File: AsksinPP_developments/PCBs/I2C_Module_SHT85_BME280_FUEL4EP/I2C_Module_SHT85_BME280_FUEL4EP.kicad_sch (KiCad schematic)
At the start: 14 parts, among them J1 Conn_01x04, J2 Conn_01x04, U1 BME280, U2 SHT85

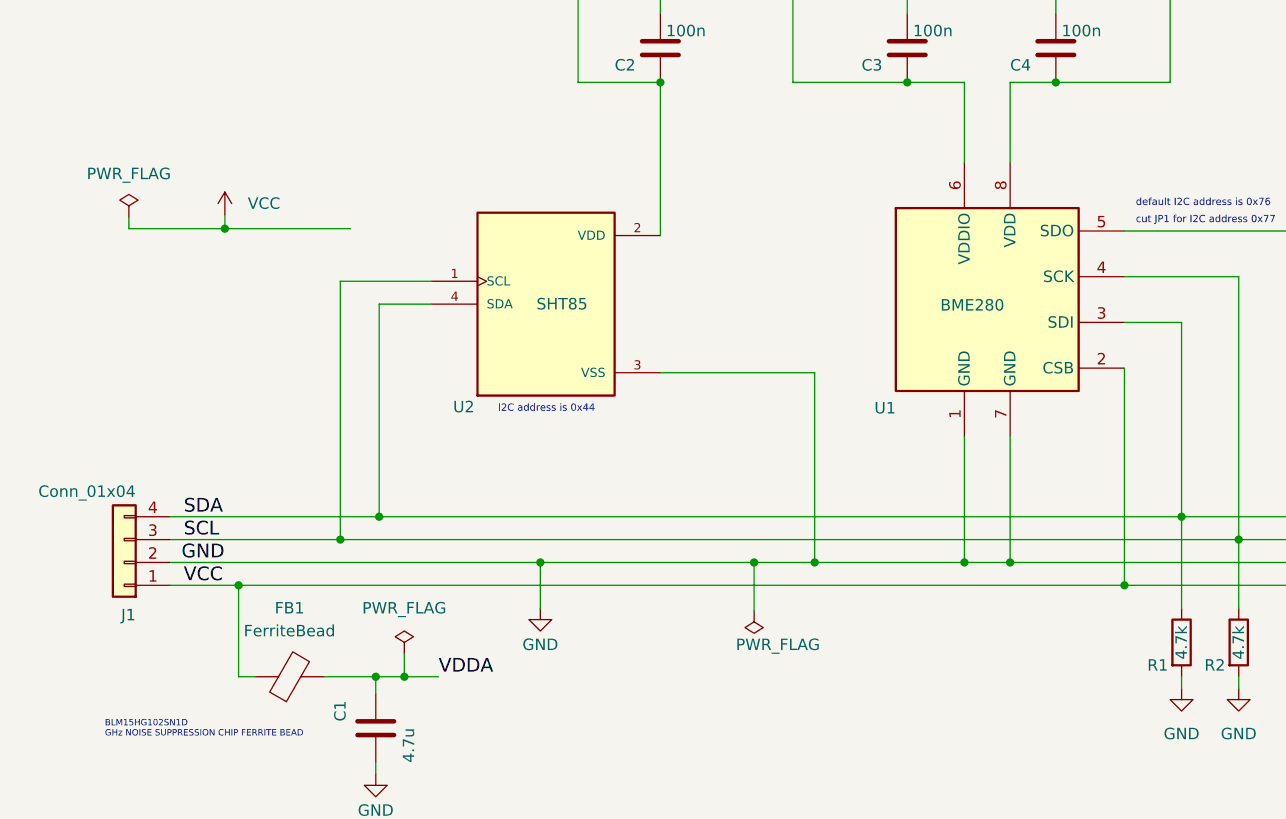
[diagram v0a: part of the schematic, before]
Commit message: PCBs: fix of some project specific KiCAD library paths for portability and missing PWR_FLGs for VCC in some schematics
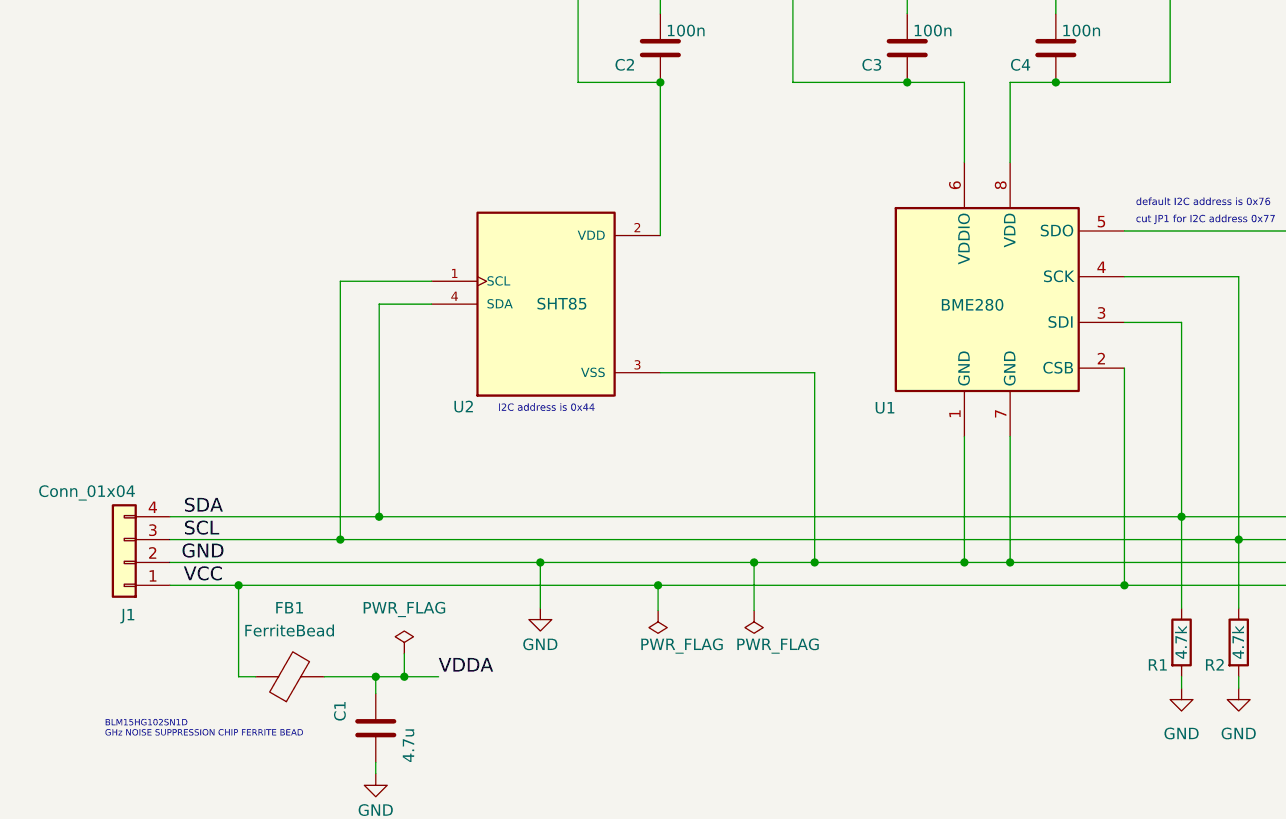
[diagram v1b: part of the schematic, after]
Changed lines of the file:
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@@
   (title_block
     (title "I2C_Module_SHT85_BME280_FUEL4EP")
-    (date "2023-09-08")
-    (rev "1.0")
+    (date "2024-01-14")
+    (rev "1.1")
     (company "FUEL4EP")
     (comment 1 "fitting to  HB-UNI-SEN-BATT_ATMega1284P_E07-868MS10_FUEL4EP")
@@
   (junction (at 149.86 111.76) (diameter 0) (color 0 0 0 0)
   )
-  (junction (at 62.611 74.676) (diameter 0) (color 0 0 0 0)
-  )
   (junction (at 154.94 58.42) (diameter 0) (color 0 0 0 0)
   )
@@
   (junction (at 110.998 58.42) (diameter 0) (color 0 0 0 0)
   )
+  (junction (at 110.744 114.3) (diameter 0) (color 0 0 0 0)
+  )
   (junction (at 190.5 74.93) (diameter 0) (color 0 0 0 0)
   )
@@
     (stroke (width 0) (type default) (color 0 0 0 0))
   )
-  (wire (pts (xy 51.943 74.676) (xy 51.943 73.406))
-    (stroke (width 0) (type default) (color 0 0 0 0))
-  )
   (wire (pts (xy 138.43 48.26) (xy 138.43 50.8))
     (stroke (width 0) (type default) (color 0 0 0 0))
@@
     (stroke (width 0) (type default) (color 0 0 0 0))
   )
-  (wire (pts (xy 62.611 74.676) (xy 51.943 74.676))
-    (stroke (width 0) (type default) (color 0 0 0 0))
-  )
   (wire (pts (xy 138.43 58.42) (xy 144.78 58.42))
     (stroke (width 0) (type default) (color 0 0 0 0))
@@
     (stroke (width 0) (type default) (color 0 0 0 0))
   )
-  (wire (pts (xy 62.611 74.676) (xy 62.611 73.152))
-    (stroke (width 0) (type default) (color 0 0 0 0))
-  )
   (wire (pts (xy 125.73 58.42) (xy 138.43 58.42))
     (stroke (width 0) (type default) (color 0 0 0 0))
   )
-  (wire (pts (xy 64.135 114.3) (xy 162.56 114.3))
+  (wire (pts (xy 64.135 114.3) (xy 110.744 114.3))
     (stroke (width 0) (type default) (color 0 0 0 0))
   )
@@
     (stroke (width 0) (type default) (color 0 0 0 0))
   )
+  (wire (pts (xy 110.744 114.3) (xy 110.744 117.094))
+    (stroke (width 0) (type default) (color 0 0 0 0))
+  )
   (wire (pts (xy 64.135 124.46) (xy 66.04 124.46))
     (stroke (width 0) (type default) (color 0 0 0 0))
@@
     (stroke (width 0) (type default) (color 0 0 0 0))
   )
-  (wire (pts (xy 62.611 74.676) (xy 76.581 74.676))
-    (stroke (width 0) (type default) (color 0 0 0 0))
-  )
   (wire (pts (xy 56.515 111.76) (xy 97.663 111.76))
     (stroke (width 0) (type default) (color 0 0 0 0))
@@
   )
   (wire (pts (xy 121.412 111.76) (xy 121.412 117.094))
+    (stroke (width 0) (type default) (color 0 0 0 0))
+  )
+  (wire (pts (xy 110.744 114.3) (xy 162.56 114.3))
     (stroke (width 0) (type default) (color 0 0 0 0))
   )
@@
     )
     (property "Datasheet" "" (id 3) (at 101.854 48.768 0)
+      (effects (font (size 1.27 1.27)) hide)
+    )
+    (pin "1")
+  )
+  (symbol (lib_id "power:PWR_FLAG") (at 110.744 117.094 180) (unit 1)
+    (in_bom yes) (on_board yes)
+    (property "Reference" "#FLG0102" (id 0) (at 110.744 118.999 0)
+      (effects (font (size 1.27 1.27)) hide)
+    )
+    (property "Value" "PWR_FLAG" (id 1) (at 108.712 120.904 0)
+      (effects (font (size 1.27 1.27)) (justify right))
+    )
+    (property "Footprint" "" (id 2) (at 110.744 117.094 0)
+      (effects (font (size 1.27 1.27)) hide)
+    )
+    (property "Datasheet" "~" (id 3) (at 110.744 117.094 0)
       (effects (font (size 1.27 1.27)) hide)
     )
@@
       (effects (font (size 1.27 1.27)) (justify bottom) hide)
     )
-    (property "Datasheet" "" (id 3) (at 98.298 83.058 0)
+    (property "Datasheet" "https://www.mouser.com/catalog/specsheets/Sensirion_10022018_HT_DS_SHT85_V0.9_D1.pdf" (id 3) (at 98.298 83.058 0)
       (effects (font (size 1.27 1.27)) hide)
     )
@@
     (pin "8")
   )
-  (symbol (lib_id "power:VCC") (at 62.611 73.152 0) (unit 1)
-    (in_bom yes) (on_board yes) (fields_autoplaced)
-    (property "Reference" "#PWR01" (id 0) (at 62.611 76.962 0)
-      (effects (font (size 1.27 1.27)) hide)
-    )
-    (property "Value" "VCC" (id 1) (at 65.151 71.8819 0)
-      (effects (font (size 1.27 1.27)) (justify left))
-    )
-    (property "Footprint" "" (id 2) (at 62.611 73.152 0)
-      (effects (font (size 1.27 1.27)) hide)
-    )
-    (property "Datasheet" "" (id 3) (at 62.611 73.152 0)
-      (effects (font (size 1.27 1.27)) hide)
-    )
-    (pin "1")
-  )
   (symbol (lib_id "Device:C") (at 79.375 130.175 0) (unit 1)
     (in_bom yes) (on_board yes)
@@
     (pin "1")
   )
-  (symbol (lib_id "power:PWR_FLAG") (at 51.943 73.406 0) (unit 1)
-    (in_bom yes) (on_board yes) (fields_autoplaced)
-    (property "Reference" "#FLG01" (id 0) (at 51.943 71.501 0)
-      (effects (font (size 1.27 1.27)) hide)
-    )
-    (property "Value" "PWR_FLAG" (id 1) (at 51.943 68.58 0))
-    (property "Footprint" "" (id 2) (at 51.943 73.406 0)
-      (effects (font (size 1.27 1.27)) hide)
-    )
-    (property "Datasheet" "~" (id 3) (at 51.943 73.406 0)
-      (effects (font (size 1.27 1.27)) hide)
-    )
-    (pin "1")
-  )
   (symbol (lib_id "power:PWR_FLAG") (at 121.412 117.094 180) (unit 1)
     (in_bom yes) (on_board yes)
@@
   )
   (symbol_instances
-    (path "/accbd0c3-e588-4a03-8c25-5dc64064deb9"
-      (reference "#FLG01") (unit 1) (value "PWR_FLAG") (footprint "")
-    )
     (path "/b998681a-aa50-4b75-bf22-d9fbe42fce6f"
       (reference "#FLG02") (unit 1) (value "PWR_FLAG") (footprint "")
@@
       (reference "#FLG0101") (unit 1) (value "PWR_FLAG") (footprint "")
     )
-    (path "/71fc455e-be46-44e1-9ad6-6659dc653656"
-      (reference "#PWR01") (unit 1) (value "VCC") (footprint "")
+    (path "/15ea65a4-8a5d-4711-ae9c-e4cab444a8d6"
+      (reference "#FLG0102") (unit 1) (value "PWR_FLAG") (footprint "")
     )
     (path "/2fb280af-9352-43f7-93d8-89326fb5dc6f"

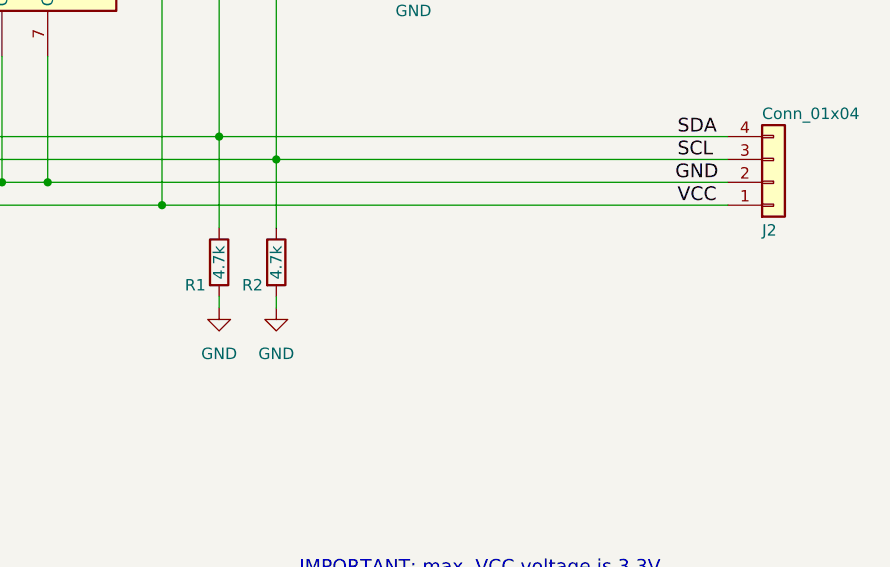
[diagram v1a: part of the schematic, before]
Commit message: PCBs: fix of I2C Pull-up resistors that were wrongly tied to GND
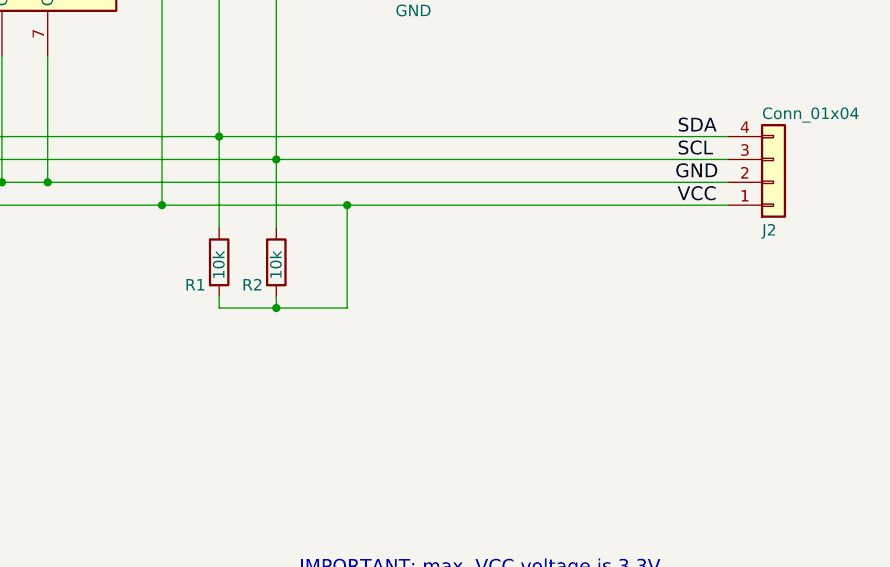
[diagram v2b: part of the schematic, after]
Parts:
- R1, R2: value 4.7k -> 10k; LCSC C25900 -> C25744
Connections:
- net GND: no longer R1.2, R2.2
- net VCC: now also R1.2, R2.2
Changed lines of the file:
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@@
   (title_block
     (title "I2C_Module_SHT85_BME280_FUEL4EP")
-    (date "2024-01-14")
-    (rev "1.1")
+    (date "2024-02-08")
+    (rev "1.2")
     (company "FUEL4EP")
     (comment 1 "fitting to  HB-UNI-SEN-BATT_ATMega1284P_E07-868MS10_FUEL4EP")
@@
   (junction (at 79.756 106.68) (diameter 0) (color 0 0 0 0)
   )
+  (junction (at 183.134 114.3) (diameter 0) (color 0 0 0 0)
+  )
   (junction (at 149.86 111.76) (diameter 0) (color 0 0 0 0)
   )
   (junction (at 154.94 58.42) (diameter 0) (color 0 0 0 0)
   )
+  (junction (at 175.26 125.73) (diameter 0) (color 0 0 0 0)
+  )
   (junction (at 128.143 111.76) (diameter 0) (color 0 0 0 0)
   )
@@
     (stroke (width 0) (type default) (color 0 0 0 0))
   )
+  (wire (pts (xy 183.134 125.73) (xy 183.134 114.3))
+    (stroke (width 0) (type default) (color 0 0 0 0))
+  )
   (wire (pts (xy 144.78 67.31) (xy 144.78 58.42))
     (stroke (width 0) (type default) (color 0 0 0 0))
@@
     (stroke (width 0) (type default) (color 0 0 0 0))
   )
+  (wire (pts (xy 175.26 125.73) (xy 183.134 125.73))
+    (stroke (width 0) (type default) (color 0 0 0 0))
+  )
   (wire (pts (xy 138.43 58.42) (xy 144.78 58.42))
     (stroke (width 0) (type default) (color 0 0 0 0))
@@
     (stroke (width 0) (type default) (color 0 0 0 0))
   )
+  (wire (pts (xy 183.134 114.3) (xy 225.425 114.3))
+    (stroke (width 0) (type default) (color 0 0 0 0))
+  )
   (wire (pts (xy 125.73 48.26) (xy 125.73 58.42))
     (stroke (width 0) (type default) (color 0 0 0 0))
@@
     (stroke (width 0) (type default) (color 0 0 0 0))
   )
-  (wire (pts (xy 162.56 114.3) (xy 225.425 114.3))
+  (wire (pts (xy 162.56 114.3) (xy 183.134 114.3))
     (stroke (width 0) (type default) (color 0 0 0 0))
   )
   (wire (pts (xy 110.998 48.768) (xy 110.998 50.8))
+    (stroke (width 0) (type default) (color 0 0 0 0))
+  )
+  (wire (pts (xy 168.91 125.73) (xy 175.26 125.73))
     (stroke (width 0) (type default) (color 0 0 0 0))
   )
@@
       (effects (font (size 1.27 1.27)) (justify left))
     )
-    (property "Value" "4.7k" (id 1) (at 168.91 122.555 90)
+    (property "Value" "10k" (id 1) (at 168.91 122.555 90)
       (effects (font (size 1.27 1.27)) (justify left))
     )
@@
       (effects (font (size 1.27 1.27)) hide)
     )
-    (property "LCSC" "C25900" (id 4) (at 168.91 120.65 0)
+    (property "LCSC" "C25744" (id 4) (at 168.91 120.65 0)
       (effects (font (size 1.524 1.524)) hide)
     )
@@
     )
     (property "Datasheet" "~" (id 3) (at 110.744 117.094 0)
-      (effects (font (size 1.27 1.27)) hide)
-    )
-    (pin "1")
-  )
-  (symbol (lib_id "power:GND") (at 168.91 125.73 0) (unit 1)
-    (in_bom yes) (on_board yes) (fields_autoplaced)
-    (property "Reference" "#PWR07" (id 0) (at 168.91 132.08 0)
-      (effects (font (size 1.27 1.27)) hide)
-    )
-    (property "Value" "GND" (id 1) (at 168.91 130.81 0))
-    (property "Footprint" "" (id 2) (at 168.91 125.73 0)
-      (effects (font (size 1.27 1.27)) hide)
-    )
-    (property "Datasheet" "" (id 3) (at 168.91 125.73 0)
       (effects (font (size 1.27 1.27)) hide)
     )
@@
     (pin "1")
   )
-  (symbol (lib_id "power:GND") (at 175.26 125.73 0) (unit 1)
-    (in_bom yes) (on_board yes) (fields_autoplaced)
-    (property "Reference" "#PWR08" (id 0) (at 175.26 132.08 0)
-      (effects (font (size 1.27 1.27)) hide)
-    )
-    (property "Value" "GND" (id 1) (at 175.26 130.81 0))
-    (property "Footprint" "" (id 2) (at 175.26 125.73 0)
-      (effects (font (size 1.27 1.27)) hide)
-    )
-    (property "Datasheet" "" (id 3) (at 175.26 125.73 0)
-      (effects (font (size 1.27 1.27)) hide)
-    )
-    (pin "1")
-  )
   (symbol (lib_id "power:VDDA") (at 167.64 48.26 0) (unit 1)
     (in_bom yes) (on_board yes) (fields_autoplaced)
@@
       (effects (font (size 1.27 1.27)) (justify left))
     )
-    (property "Value" "4.7k" (id 1) (at 175.26 122.555 90)
+    (property "Value" "10k" (id 1) (at 175.26 122.555 90)
       (effects (font (size 1.27 1.27)) (justify left))
     )
@@
       (effects (font (size 1.27 1.27)) hide)
     )
-    (property "LCSC" "C25900" (id 4) (at 175.26 120.65 0)
+    (property "LCSC" "C25744" (id 4) (at 175.26 120.65 0)
       (effects (font (size 1.524 1.524)) hide)
     )
@@
       (reference "#PWR06") (unit 1) (value "VDDA") (footprint "")
     )
-    (path "/18542ab6-239f-4332-a70c-3c8551b285bb"
-      (reference "#PWR07") (unit 1) (value "GND") (footprint "")
-    )
-    (path "/d43541cc-8fb7-4c57-a7c8-5b5588c55acf"
-      (reference "#PWR08") (unit 1) (value "GND") (footprint "")
-    )
     (path "/b9ee5250-0210-4fd4-abf8-6419214a066d"
       (reference "#PWR09") (unit 1) (value "GND") (footprint "")
@@
     )
     (path "/010452d5-e5f2-447e-a153-71da0dbec114"
-      (reference "R1") (unit 1) (value "4.7k") (footprint "Resistor_SMD:R_0402_1005Metric")
+      (reference "R1") (unit 1) (value "10k") (footprint "Resistor_SMD:R_0402_1005Metric")
     )
     (path "/f75dc7be-70bf-4119-8c06-195e1a960dd2"
-      (reference "R2") (unit 1) (value "4.7k") (footprint "Resistor_SMD:R_0402_1005Metric")
+      (reference "R2") (unit 1) (value "10k") (footprint "Resistor_SMD:R_0402_1005Metric")
     )
     (path "/55b96afd-ec19-4400-9134-cc56302d872a"
